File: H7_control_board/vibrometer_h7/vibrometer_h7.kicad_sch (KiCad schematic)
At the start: 0 parts

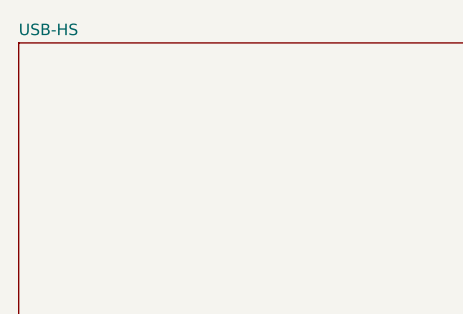
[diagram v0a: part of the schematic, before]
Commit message: added cubeIDE projects
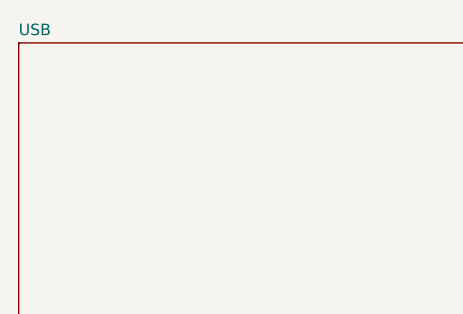
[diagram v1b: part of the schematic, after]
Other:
- sheet USB-HS renamed USB
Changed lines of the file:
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@@
 			(color 0 0 0 0.0000)
 		)
-		(property "Sheetname" "USB-HS"
+		(property "Sheetname" "USB"
 			(at 38.1 37.3884 0)
 			(effects

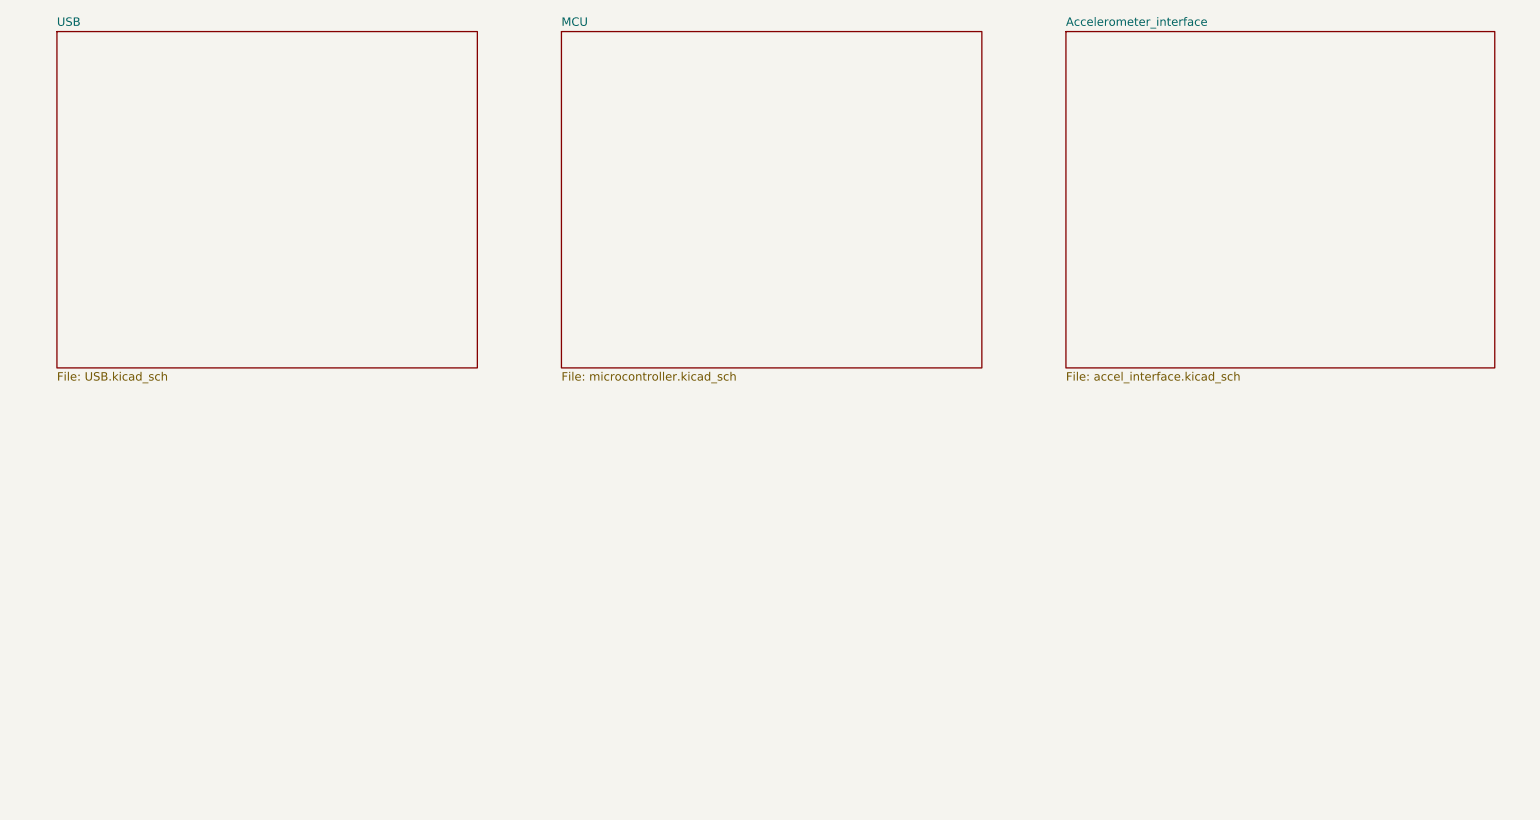
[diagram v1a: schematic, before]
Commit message: added UI leds to schematic
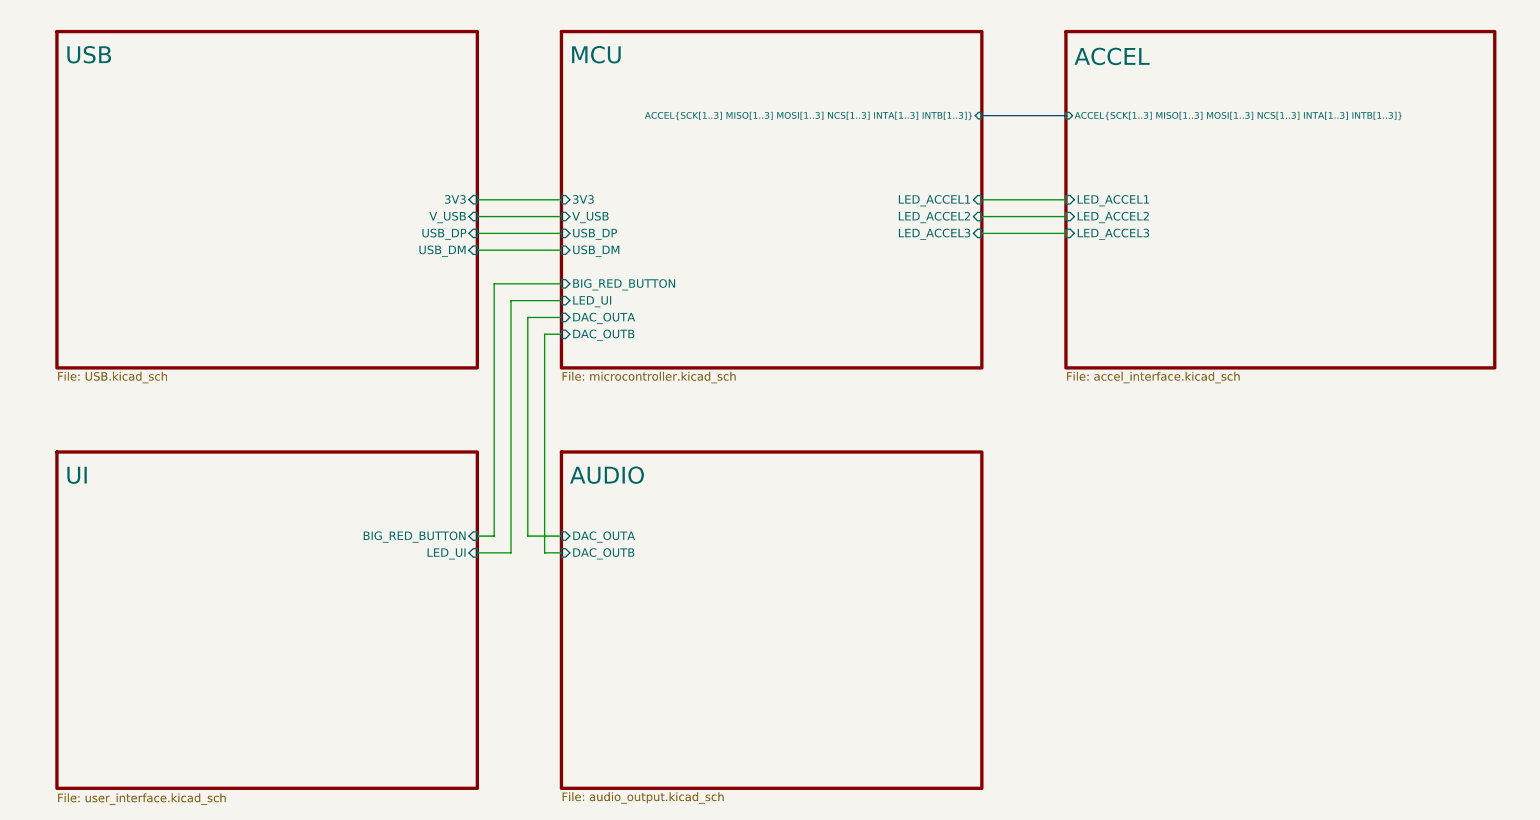
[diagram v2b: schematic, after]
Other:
- sheet Accelerometer_interface renamed ACCEL
- added sheet AUDIO (audio_output.kicad_sch)
- added sheet UI (user_interface.kicad_sch)
- sheet ACCEL ports: added ACCEL{SCK[1..3] MISO[1..3] MOSI[1..3] NCS[1..3] INTA[1..3] INTB[1..3]}, LED_ACCEL1, LED_ACCEL2, LED_ACCEL3; removed none
- sheet MCU ports: added 3V3, ACCEL{SCK[1..3] MISO[1..3] MOSI[1..3] NCS[1..3] INTA[1..3] INTB[1..3]}, BIG_RED_BUTTON, DAC_OUTA, DAC_OUTB, LED_ACCEL1, LED_ACCEL2, LED_ACCEL3, LED_UI, USB_DM, USB_DP, V_USB; removed none
- sheet USB ports: added 3V3, USB_DM, USB_DP, V_USB; removed none

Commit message: adding strobe light to board itself
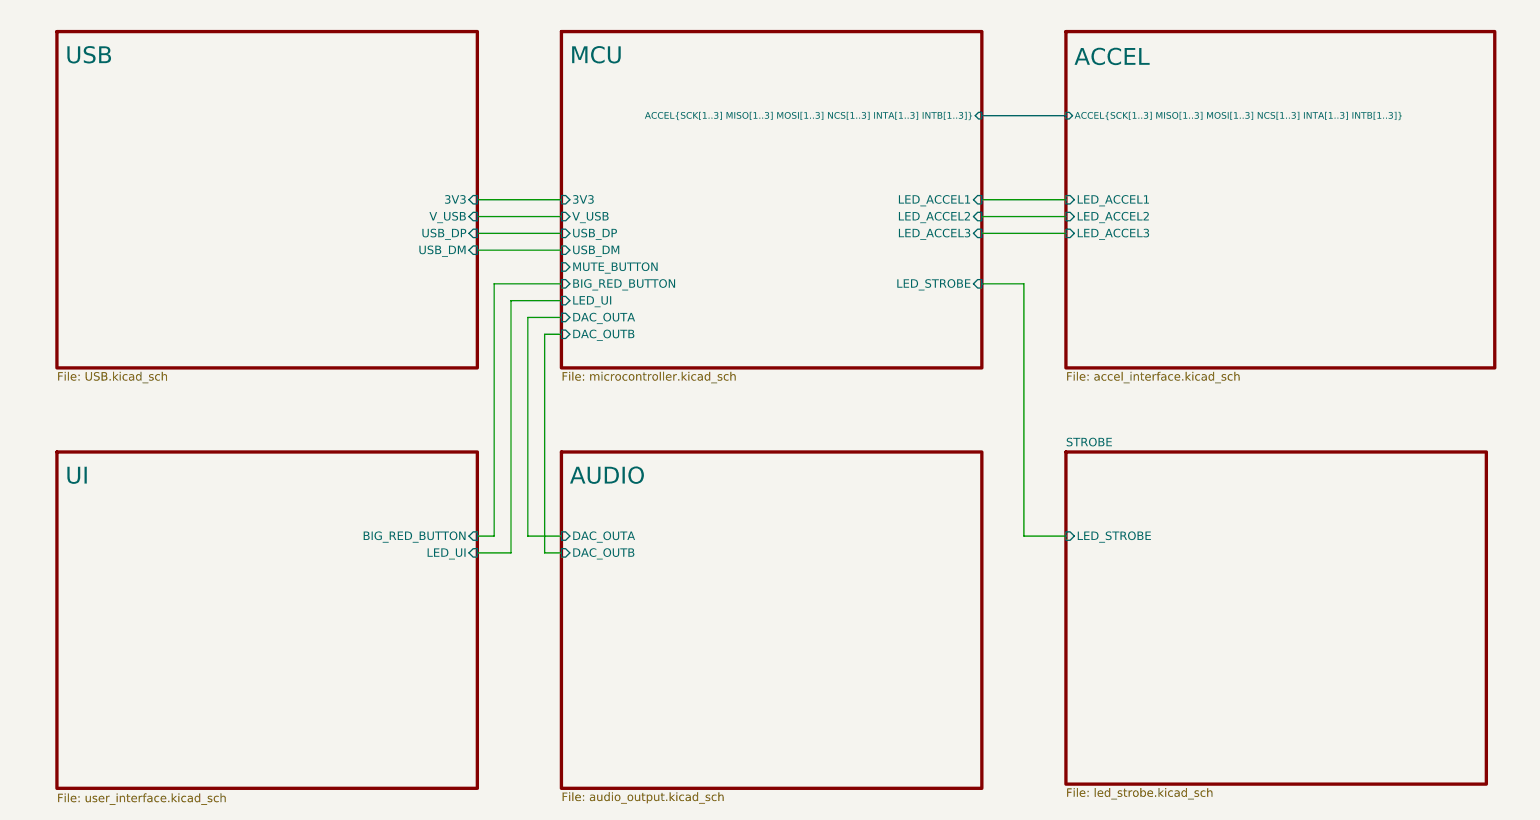
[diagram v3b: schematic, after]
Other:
- added sheet STROBE (led_strobe.kicad_sch)
- sheet MCU ports: added LED_STROBE, MUTE_BUTTON; removed none
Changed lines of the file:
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@@
+	(wire
+		(pts
+			(xy 184.15 114.3) (xy 190.5 114.3)
+		)
+		(stroke
+			(width 0)
+			(type default)
+		)
+	)
 	(wire
 		(pts
@@
 		(pts
 			(xy 177.8 50.8) (xy 190.5 50.8)
+		)
+		(stroke
+			(width 0)
+			(type default)
+		)
+	)
+	(wire
+		(pts
+			(xy 184.15 76.2) (xy 184.15 114.3)
+		)
+		(stroke
+			(width 0)
+			(type default)
+		)
+	)
+	(wire
+		(pts
+			(xy 177.8 76.2) (xy 184.15 76.2)
 		)
 		(stroke
@@
 		(pin "DAC_OUTB" input
 			(at 114.3 83.82 180)
+			(effects
+				(font
+					(size 1.27 1.27)
+				)
+				(justify left)
+			)
+		)
+		(pin "LED_STROBE" input
+			(at 177.8 76.2 0)
+			(effects
+				(font
+					(size 1.27 1.27)
+				)
+				(justify right)
+			)
+		)
+		(pin "MUTE_BUTTON" input
+			(at 114.3 73.66 180)
 			(effects
 				(font
@@
 				)
 			)
+		)
+	)
+	(sheet
+		(at 190.5 101.6)
+		(size 63.5 50.165)
+		(fields_autoplaced yes)
+		(stroke
+			(width 0.5)
+			(type solid)
+		)
+		(fill
+			(color 255 220 173 0.5020)
+		)
+		(property "Sheetname" "STROBE"
+			(at 190.5 100.8884 0)
+			(effects
+				(font
+					(size 1.27 1.27)
+				)
+				(justify left bottom)
+			)
+		)
+		(property "Sheetfile" "led_strobe.kicad_sch"
+			(at 190.5 152.3496 0)
+			(effects
+				(font
+					(size 1.27 1.27)
+				)
+				(justify left top)
+			)
+		)
+		(property "Field2" ""
+			(at 190.5 101.6 0)
+			(effects
+				(font
+					(size 1.27 1.27)
+				)
+				(hide yes)
+			)
+		)
+		(pin "LED_STROBE" input
+			(at 190.5 114.3 180)
+			(effects
+				(font
+					(size 1.27 1.27)
+				)
+				(justify left)
+			)
+		)
+		(instances
+			(project "vibrometer_h7"
+				(path "/18de6987-156a-4b34-871e-cbbe1d261986"
+					(page "10")
+				)
+			)

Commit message: worked on audio output stuff, cleaned schematic
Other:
- sheet ACCEL ports: added LED_ACCEL; removed LED_ACCEL1, LED_ACCEL2, LED_ACCEL3
- sheet AUDIO ports: added MUTE_SIGNAL; removed none
- sheet MCU ports: added LED_ACCEL, MUTE_SIGNAL; removed LED_ACCEL1, LED_ACCEL2, LED_ACCEL3
- sheet UI ports: added MUTE_BUTTON; removed none

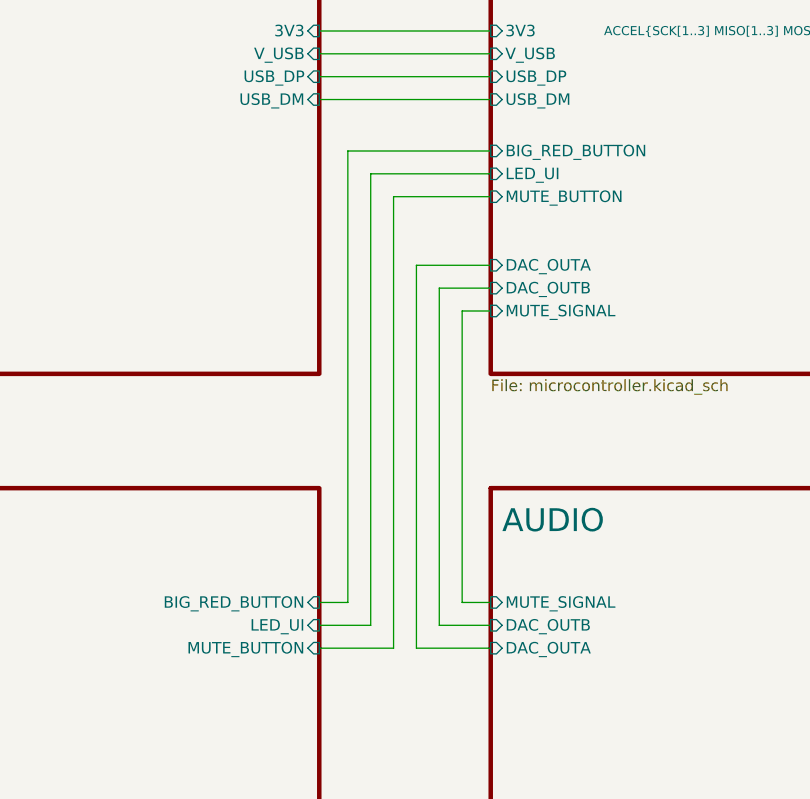
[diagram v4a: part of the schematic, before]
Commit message: met with john to go over schematic. made changes, got rid of some leds...
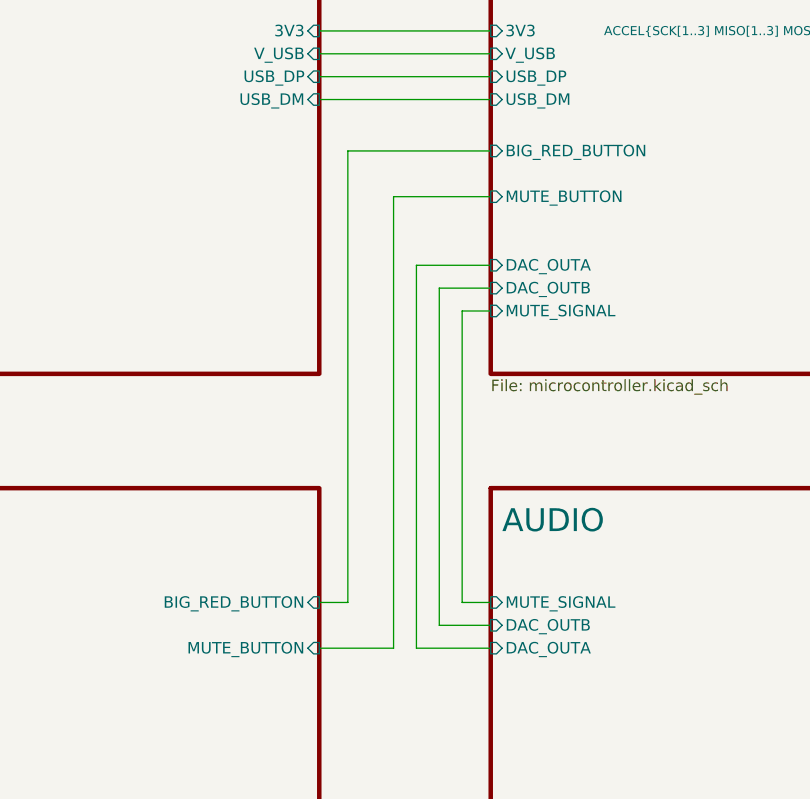
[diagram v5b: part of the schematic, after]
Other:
- sheet MCU ports: added none; removed LED_UI
- sheet UI ports: added none; removed LED_UI
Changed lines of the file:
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@@
-	(wire
-		(pts
-			(xy 100.965 66.675) (xy 100.965 116.84)
-		)
-		(stroke
-			(width 0)
-			(type default)
-		)
-	)
 	(wire
 		(pts
@@
 	(wire
 		(pts
-			(xy 100.965 116.84) (xy 95.25 116.84)
-		)
-		(stroke
-			(width 0)
-			(type default)
-		)
-	)
-	(wire
-		(pts
 			(xy 114.3 64.135) (xy 98.425 64.135)
 		)
@@
 		(pts
 			(xy 106.045 76.835) (xy 106.045 119.38)
-		)
-		(stroke
-			(width 0)
-			(type default)
-		)
-	)
-	(wire
-		(pts
-			(xy 114.3 66.675) (xy 100.965 66.675)
 		)
 		(stroke
@@
 				)
 				(justify left top)
-			)
-		)
-		(pin "LED_UI" input
-			(at 114.3 66.675 180)
-			(effects
-				(font
-					(size 1.27 1.27)
-				)
-				(justify left)
 			)
 		)
@@
 			(effects
 				(font
-					(size 1.27 1.27)
-				)
-				(justify right)
-			)
-		)
-		(pin "LED_UI" input
-			(at 95.25 116.84 0)
-			(effects
-				(font

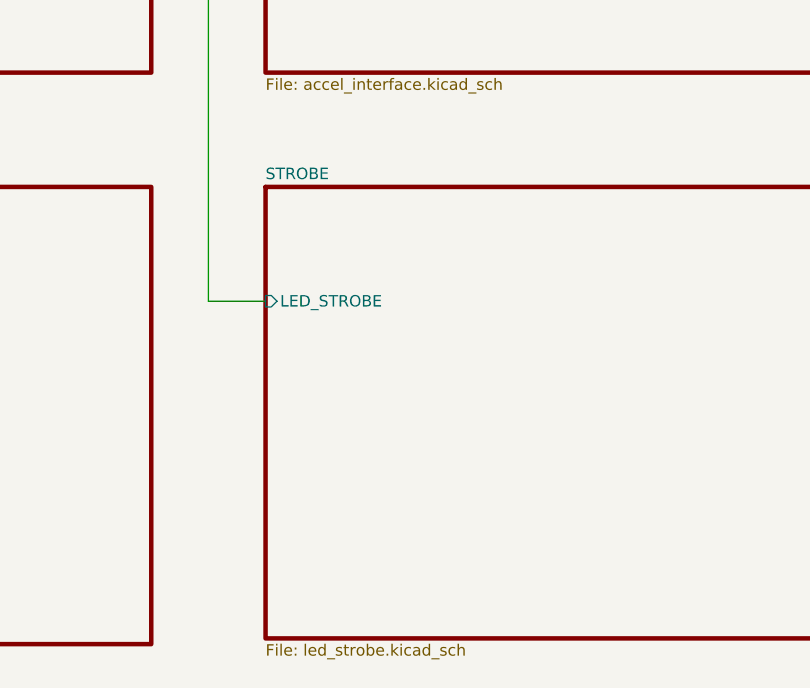
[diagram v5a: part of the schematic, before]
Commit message: added notes about LED drive component selection
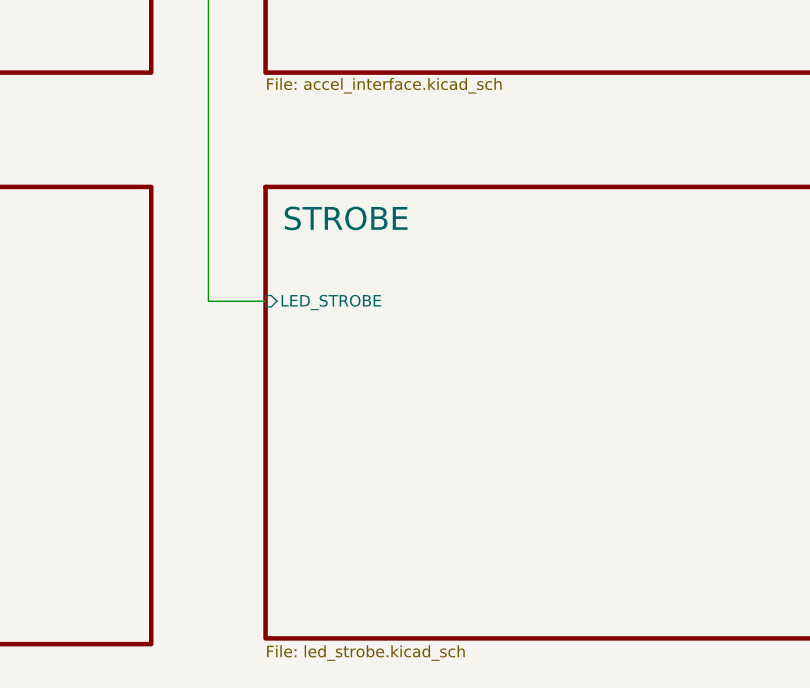
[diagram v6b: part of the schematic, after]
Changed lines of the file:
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@@
 		(at 190.5 101.6)
 		(size 63.5 50.165)
-		(fields_autoplaced yes)
 		(stroke
 			(width 0.5)
@@
 		)
 		(property "Sheetname" "STROBE"
-			(at 190.5 100.8884 0)
+			(at 192.405 106.68 0)
 			(effects
 				(font
-					(size 1.27 1.27)
+					(size 2.54 2.54)
 				)
 				(justify left bottom)
@@
 		)
 		(property "Sheetfile" "led_strobe.kicad_sch"
-			(at 190.5 152.3496 0)
+			(at 190.5 152.5234 0)
 			(effects
 				(font
